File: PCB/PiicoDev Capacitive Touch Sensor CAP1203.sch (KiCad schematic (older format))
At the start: 35 parts, among them J1 , J11 Conn_01x01_Male, J12 Conn_01x01_Male, J13 Conn_01x01_Male, J2 , J3 Conn_PiicoDev_header_01x04_Ma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, J4 Conn_01x01_Male, J5 Conn_01x01_Male, J6 Conn_01x01_Male, J7 Conn_01x01_Male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

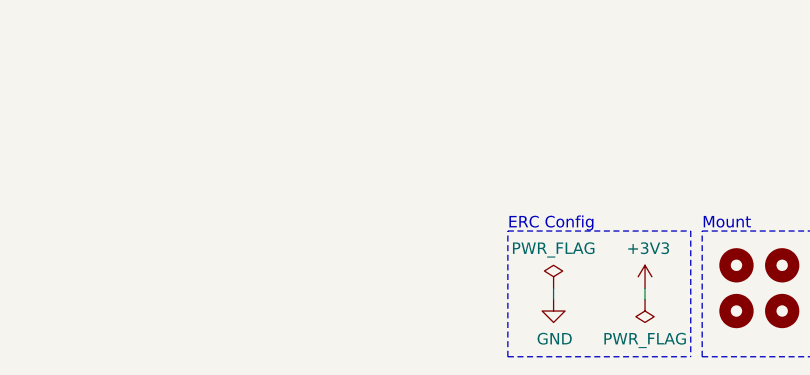
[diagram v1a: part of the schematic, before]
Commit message: Add silk screen labels
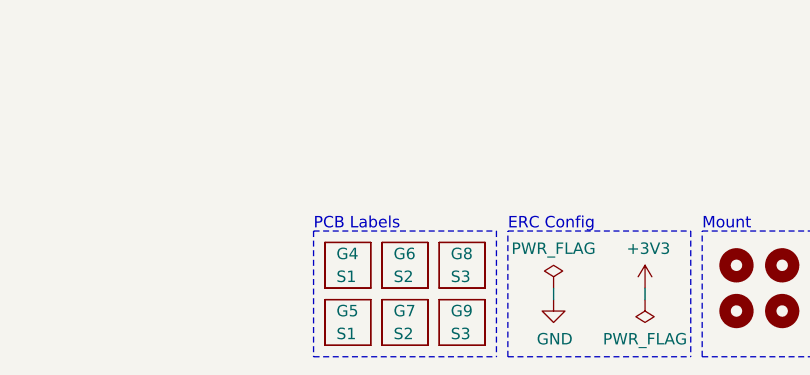
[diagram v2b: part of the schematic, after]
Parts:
- added G4, G5: S1, PiicoDev Capacitive Touch Sensor CAP1203:Label_S1_Reverse, symbol CoreElectronics_Artwork:Label_PCB_Art
- added G6, G7: S2, PiicoDev Capacitive Touch Sensor CAP1203:Label_S2_Reverse, symbol CoreElectronics_Artwork:Label_PCB_Art
- added G8, G9: S3, PiicoDev Capacitive Touch Sensor CAP1203:Label_S3_Reverse, symbol CoreElectronics_Artwork:Label_PCB_Art
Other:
- note added: "PCB Labels"
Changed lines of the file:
@@
 Sheet 1 1
 Title "PiicoDev Capacitive Touch Sensor CAP1203"
-Date "2021-06-09"
-Rev "01"
+Date "2021-06-21"
+Rev "02"
 Comp "Core Electronics"
 Comment1 "Designed at Core Electronics by Peter Johnston"
@@
 	1    0    0    -1
 $EndComp
+$Comp
+L CoreElectronics_Artwork:Label_PCB_Art G5
+U 1 1 60D07939
+P 4450 7600
+F 0 "G5" H 4400 7650 50  0000 L CNN
+F 1 "S1" H 4400 7550 50  0000 L CNN
+F 2 "PiicoDev Capacitive Touch Sensor CAP1203:Label_S1_Reverse" H 4450 7600 50  0001 C CNN
+F 3 "" H 4450 7600 50  0001 C CNN
+	1    4450 7600
+	1    0    0    -1
+$EndComp
+$Comp
+L CoreElectronics_Artwork:Label_PCB_Art G4
+U 1 1 60D089C5
+P 4450 7350
+F 0 "G4" H 4400 7400 50  0000 L CNN
+F 1 "S1" H 4400 7300 50  0000 L CNN
+F 2 "PiicoDev Capacitive Touch Sensor CAP1203:Label_S1_Reverse" H 4450 7350 50  0001 C CNN
+F 3 "" H 4450 7350 50  0001 C CNN
+	1    4450 7350
+	1    0    0    -1
+$EndComp
+$Comp
+L CoreElectronics_Artwork:Label_PCB_Art G6
+U 1 1 60D106CB
+P 4700 7350
+F 0 "G6" H 4650 7400 50  0000 L CNN
+F 1 "S2" H 4650 7300 50  0000 L CNN
+F 2 "PiicoDev Capacitive Touch Sensor CAP1203:Label_S2_Reverse" H 4700 7350 50  0001 C CNN
+F 3 "" H 4700 7350 50  0001 C CNN
+	1    4700 7350
+	1    0    0    -1
+$EndComp
+$Comp
+L CoreElectronics_Artwork:Label_PCB_Art G7
+U 1 1 60D111CB
+P 4700 7600
+F 0 "G7" H 4650 7650 50  0000 L CNN
+F 1 "S2" H 4650 7550 50  0000 L CNN
+F 2 "PiicoDev Capacitive Touch Sensor CAP1203:Label_S2_Reverse" H 4700 7600 50  0001 C CNN
+F 3 "" H 4700 7600 50  0001 C CNN
+	1    4700 7600
+	1    0    0    -1
+$EndComp
+$Comp
+L CoreElectronics_Artwork:Label_PCB_Art G8
+U 1 1 60D11A2F
+P 4950 7350
+F 0 "G8" H 4900 7400 50  0000 L CNN
+F 1 "S3" H 4900 7300 50  0000 L CNN
+F 2 "PiicoDev Capacitive Touch Sensor CAP1203:Label_S3_Reverse" H 4950 7350 50  0001 C CNN
+F 3 "" H 4950 7350 50  0001 C CNN
+	1    4950 7350
+	1    0    0    -1
+$EndComp
+$Comp
+L CoreElectronics_Artwork:Label_PCB_Art G9
+U 1 1 60D121E9
+P 4950 7600
+F 0 "G9" H 4900 7650 50  0000 L CNN
+F 1 "S3" H 4900 7550 50  0000 L CNN
+F 2 "PiicoDev Capacitive Touch Sensor CAP1203:Label_S3_Reverse" H 4950 7600 50  0001 C CNN
+F 3 "" H 4950 7600 50  0001 C CNN
+	1    4950 7600
+	1    0    0    -1
+$EndComp
+Wire Notes Line
+	5100 7200 5100 7750
+Text Notes 4300 7200 0    50   ~ 0
+PCB Labels
+Wire Notes Line
+	4300 7200 4300 7750
+Wire Notes Line
+	4300 7200 5100 7200
+Wire Notes Line
+	4300 7750 5100 7750
 $EndSCHEMATC

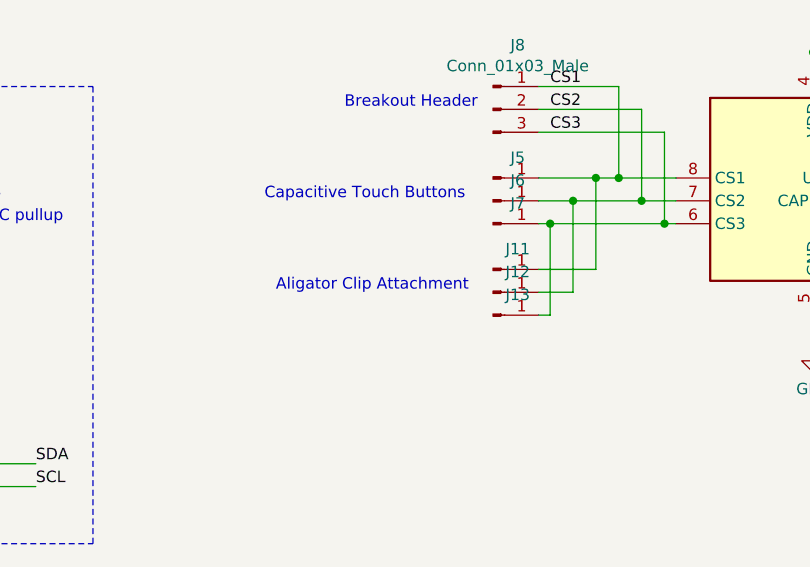
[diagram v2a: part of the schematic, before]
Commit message: Increase Alligator Clip Size
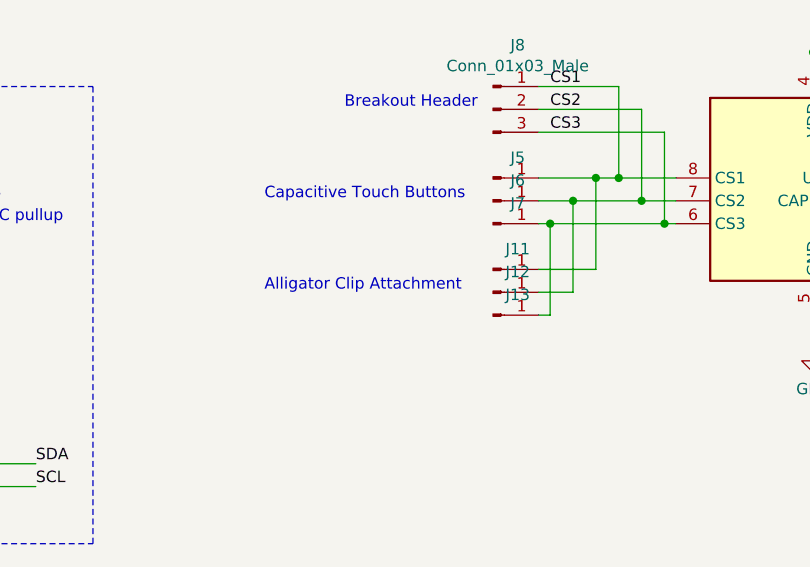
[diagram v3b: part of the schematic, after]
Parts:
- J11, J12, J13: footprint CoreElectronics_Components:Conn_alligator-banana_small -> CoreElectronics_Components:Conn_alligator
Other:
- note added: "Alligator Clip Attachment"
- note removed: "Aligator Clip Attachment"
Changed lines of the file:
@@
 Sheet 1 1
 Title "PiicoDev Capacitive Touch Sensor CAP1203"
-Date "2021-06-21"
+Date "2021-06-24"
 Rev "02"
 Comp "Core Electronics"
@@
 F 0 "J11" H 5808 3889 50  0000 C CNN
 F 1 "Conn_01x01_Male" H 5808 3890 50  0001 C CNN
-F 2 "CoreElectronics_Components:Conn_alligator-banana_small" H 5700 3800 50  0001 C CNN
+F 2 "CoreElectronics_Components:Conn_alligator" H 5700 3800 50  0001 C CNN
 F 3 "~" H 5700 3800 50  0001 C CNN
 	1    5700 3800
@@
 F 0 "J12" H 5808 3989 50  0000 C CNN
 F 1 "Conn_01x01_Male" H 5808 3990 50  0001 C CNN
-F 2 "CoreElectronics_Components:Conn_alligator-banana_small" H 5700 3900 50  0001 C CNN
+F 2 "CoreElectronics_Components:Conn_alligator" H 5700 3900 50  0001 C CNN
 F 3 "~" H 5700 3900 50  0001 C CNN
 	1    5700 3900
@@
 F 0 "J13" H 5808 4089 50  0000 C CNN
 F 1 "Conn_01x01_Male" H 5808 4090 50  0001 C CNN
-F 2 "CoreElectronics_Components:Conn_alligator-banana_small" H 5700 4000 50  0001 C CNN
+F 2 "CoreElectronics_Components:Conn_alligator" H 5700 4000 50  0001 C CNN
 F 3 "~" H 5700 4000 50  0001 C CNN
 	1    5700 4000
@@
 Text Notes 5050 3100 0    50   ~ 0
 Breakout Header
-Text Notes 4750 3900 0    50   ~ 0
-Aligator Clip Attachment
+Text Notes 4700 3900 0    50   ~ 0
+Alligator Clip Attachment
 $Comp
 L Jumper:SolderJumper_2_Bridged JP4

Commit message: Change R1 resistor value
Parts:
- R1: value 1k -> 4k7
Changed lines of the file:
@@
 AR Path="/60B035C6" Ref="R1"  Part="1"
 F 0 "R1" H 1520 3996 50  0000 L CNN
-F 1 "1k" H 1520 3905 50  0000 L CNN
+F 1 "4k7" H 1520 3905 50  0000 L CNN
 F 2 "Resistor_SMD:R_0402_1005Metric" V 1380 3950 50  0001 C CNN
 F 3 "~" H 1450 3950 50  0001 C CNN

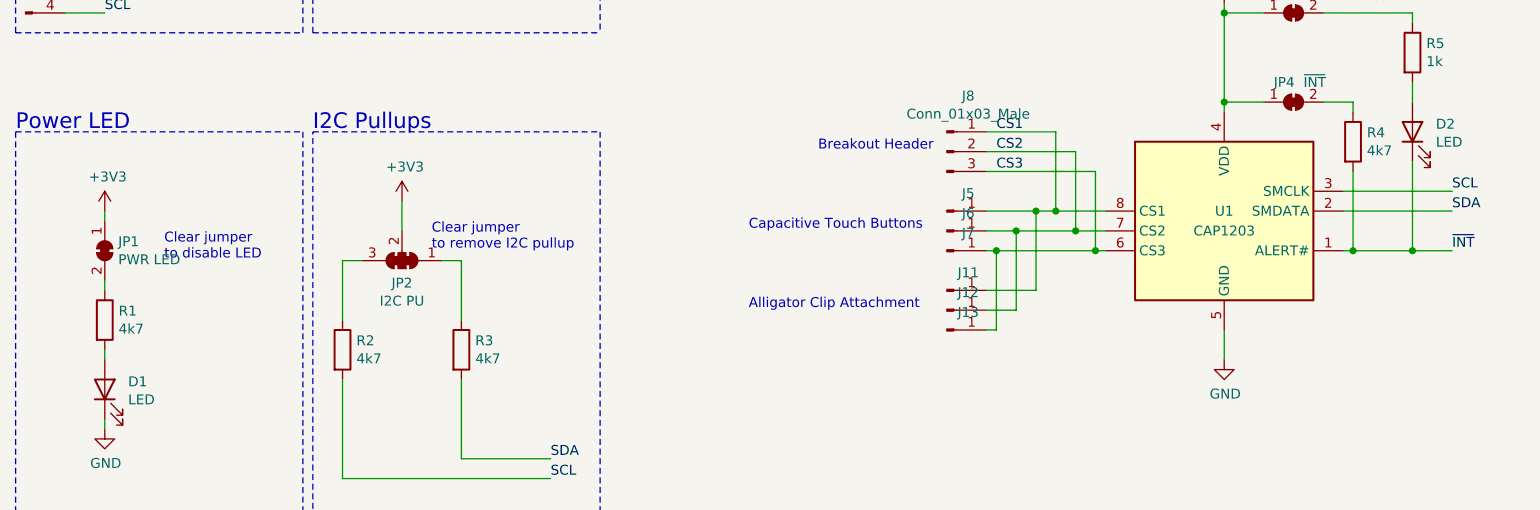
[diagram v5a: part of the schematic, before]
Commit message: Update R1,2,3,4 to 10k
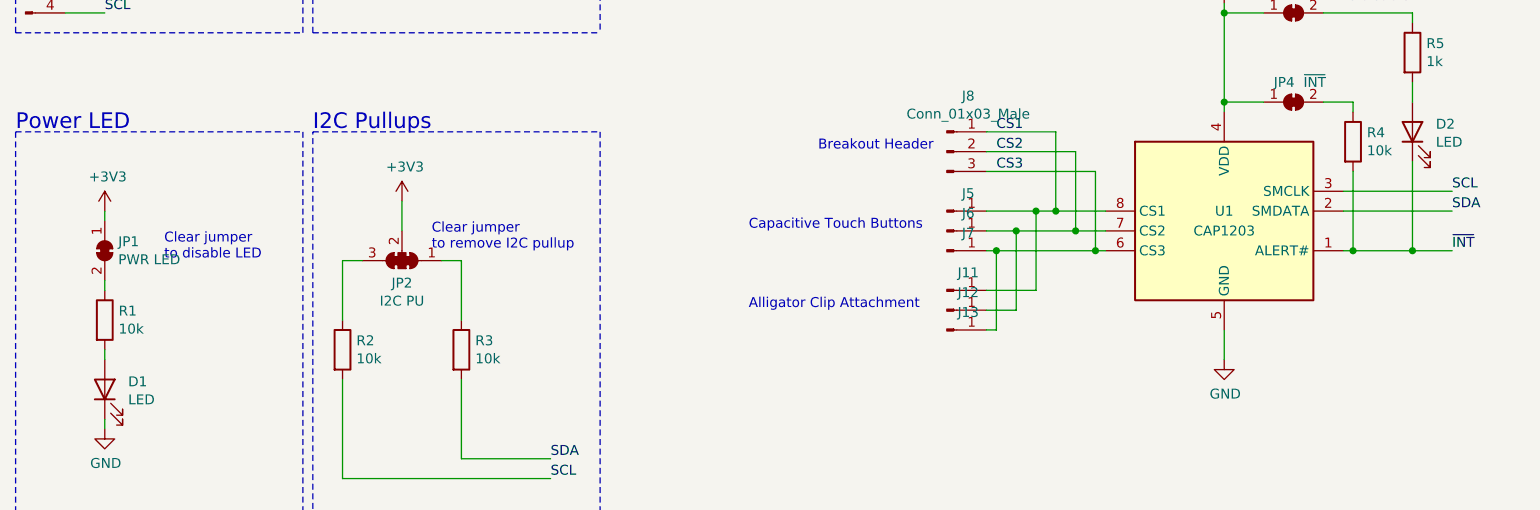
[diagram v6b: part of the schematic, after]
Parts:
- R1, R2, R3, R4: value 4k7 -> 10k
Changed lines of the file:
@@
 P 5350 7450
 AR Path="/609C5735/609C9ECA" Ref="#FLG?"  Part="1"
-AR Path="/609C9ECA" Ref="#FLG0101"  Part="1"
-F 0 "#FLG0101" H 5350 7525 50  0001 C CNN
+AR Path="/609C9ECA" Ref="#FLG?"  Part="1"
+F 0 "#FLG?" H 5350 7525 50  0001 C CNN
 F 1 "PWR_FLAG" H 5350 7623 50  0000 C CNN
 F 2 "" H 5350 7450 50  0001 C CNN
@@
 P 5750 7500
 AR Path="/609C5735/609C9ED0" Ref="#FLG?"  Part="1"
-AR Path="/609C9ED0" Ref="#FLG0102"  Part="1"
-F 0 "#FLG0102" H 5750 7575 50  0001 C CNN
+AR Path="/609C9ED0" Ref="#FLG?"  Part="1"
+F 0 "#FLG?" H 5750 7575 50  0001 C CNN
 F 1 "PWR_FLAG" H 5750 7673 50  0000 C CNN
 F 2 "" H 5750 7500 50  0001 C CNN
@@
 P 5350 7500
 AR Path="/609C5735/609C9ED6" Ref="#PWR?"  Part="1"
-AR Path="/609C9ED6" Ref="#PWR0101"  Part="1"
-F 0 "#PWR0101" H 5350 7250 50  0001 C CNN
+AR Path="/609C9ED6" Ref="#PWR?"  Part="1"
+F 0 "#PWR?" H 5350 7250 50  0001 C CNN
 F 1 "GND" H 5355 7327 50  0000 C CNN
 F 2 "" H 5350 7500 50  0001 C CNN
@@
 P 5750 7450
 AR Path="/609C5735/609C9EDC" Ref="#PWR?"  Part="1"
-AR Path="/609C9EDC" Ref="#PWR0102"  Part="1"
-F 0 "#PWR0102" H 5750 7300 50  0001 C CNN
+AR Path="/609C9EDC" Ref="#PWR?"  Part="1"
+F 0 "#PWR?" H 5750 7300 50  0001 C CNN
 F 1 "+3V3" H 5765 7623 50  0000 C CNN
 F 2 "" H 5750 7450 50  0001 C CNN
@@
 P 1600 1400
 AR Path="/609C5735/609F9AF4" Ref="#PWR?"  Part="1"
-AR Path="/609F9AF4" Ref="#PWR0103"  Part="1"
-F 0 "#PWR0103" H 1600 1250 50  0001 C CNN
+AR Path="/609F9AF4" Ref="#PWR?"  Part="1"
+F 0 "#PWR?" H 1600 1250 50  0001 C CNN
 F 1 "+3V3" V 1615 1528 50  0000 L CNN
 F 2 "" H 1600 1400 50  0001 C CNN
@@
 P 1600 1300
 AR Path="/609C5735/609F9AFA" Ref="#PWR?"  Part="1"
-AR Path="/609F9AFA" Ref="#PWR0104"  Part="1"
-F 0 "#PWR0104" H 1600 1050 50  0001 C CNN
+AR Path="/609F9AFA" Ref="#PWR?"  Part="1"
+F 0 "#PWR?" H 1600 1050 50  0001 C CNN
 F 1 "GND" V 1605 1172 50  0000 R CNN
 F 2 "" H 1600 1300 50  0001 C CNN
@@
 P 1600 2200
 AR Path="/609C5735/609F9B0C" Ref="#PWR?"  Part="1"
-AR Path="/609F9B0C" Ref="#PWR0105"  Part="1"
-F 0 "#PWR0105" H 1600 2050 50  0001 C CNN
+AR Path="/609F9B0C" Ref="#PWR?"  Part="1"
+F 0 "#PWR?" H 1600 2050 50  0001 C CNN
 F 1 "+3V3" V 1615 2328 50  0000 L CNN
 F 2 "" H 1600 2200 50  0001 C CNN
@@
 P 1600 2100
 AR Path="/609C5735/609F9B12" Ref="#PWR?"  Part="1"
-AR Path="/609F9B12" Ref="#PWR0106"  Part="1"
-F 0 "#PWR0106" H 1600 1850 50  0001 C CNN
+AR Path="/609F9B12" Ref="#PWR?"  Part="1"
+F 0 "#PWR?" H 1600 1850 50  0001 C CNN
 F 1 "GND" V 1605 1972 50  0000 R CNN
 F 2 "" H 1600 2100 50  0001 C CNN
@@
 P 3300 1400
 AR Path="/609C5735/609F9B1E" Ref="#PWR?"  Part="1"
-AR Path="/609F9B1E" Ref="#PWR0107"  Part="1"
-F 0 "#PWR0107" H 3300 1250 50  0001 C CNN
+AR Path="/609F9B1E" Ref="#PWR?"  Part="1"
+F 0 "#PWR?" H 3300 1250 50  0001 C CNN
 F 1 "+3V3" V 3315 1528 50  0000 L CNN
 F 2 "" H 3300 1400 50  0001 C CNN
@@
 P 3300 1300
 AR Path="/609C5735/609F9B24" Ref="#PWR?"  Part="1"
-AR Path="/609F9B24" Ref="#PWR0108"  Part="1"
-F 0 "#PWR0108" H 3300 1050 50  0001 C CNN
+AR Path="/609F9B24" Ref="#PWR?"  Part="1"
+F 0 "#PWR?" H 3300 1050 50  0001 C CNN
 F 1 "GND" V 3305 1172 50  0000 R CNN
 F 2 "" H 3300 1300 50  0001 C CNN
@@
 AR Path="/60A08162" Ref="R3"  Part="1"
 F 0 "R3" H 3320 4146 50  0000 L CNN
-F 1 "4k7" H 3320 4055 50  0000 L CNN
+F 1 "10k" H 3320 4055 50  0000 L CNN
 F 2 "Resistor_SMD:R_0402_1005Metric" V 3180 4100 50  0001 C CNN
 F 3 "~" H 3250 4100 50  0001 C CNN
@@
 AR Path="/60A08170" Ref="R2"  Part="1"
 F 0 "R2" H 2720 4146 50  0000 L CNN
-F 1 "4k7" H 2720 4055 50  0000 L CNN
+F 1 "10k" H 2720 4055 50  0000 L CNN
 F 2 "Resistor_SMD:R_0402_1005Metric" V 2580 4100 50  0001 C CNN
 F 3 "~" H 2650 4100 50  0001 C CNN
@@
 P 2950 3350
 AR Path="/609C5735/60A0817C" Ref="#PWR?"  Part="1"
-AR Path="/60A0817C" Ref="#PWR0109"  Part="1"
-F 0 "#PWR0109" H 2950 3200 50  0001 C CNN
+AR Path="/60A0817C" Ref="#PWR?"  Part="1"
+F 0 "#PWR?" H 2950 3200 50  0001 C CNN
 F 1 "+3V3" H 2965 3523 50  0000 C CNN
 F 2 "" H 2950 3350 50  0001 C CNN
@@
 	1000 5000 2450 5000
 $Comp
-L power:+3V3 #PWR0112
+L power:+3V3 #PWR?
 U 1 1 60A58B8E
 P 7100 2350
-F 0 "#PWR0112" H 7100 2200 50  0001 C CNN
+F 0 "#PWR?" H 7100 2200 50  0001 C CNN
 F 1 "+3V3" H 7115 2523 50  0000 C CNN
 F 2 "" H 7100 2350 50  0001 C CNN
@@
 ~INT
 $Comp
-L power:GND #PWR0113
+L power:GND #PWR?
 U 1 1 60A63B22
 P 7100 4150
-F 0 "#PWR0113" H 7100 3900 50  0001 C CNN
+F 0 "#PWR?" H 7100 3900 50  0001 C CNN
 F 1 "GND" H 7105 3977 50  0000 C CNN
 F 2 "" H 7100 4150 50  0001 C CNN
@@
 Connection ~ 9000 3700
 $Comp
-L power:GND #PWR0114
+L power:GND #PWR?
 U 1 1 60A78BAC
 P 9000 4150
-F 0 "#PWR0114" H 9000 3900 50  0001 C CNN
+F 0 "#PWR?" H 9000 3900 50  0001 C CNN
 F 1 "GND" H 9005 3977 50  0000 C CNN
 F 2 "" H 9000 4150 50  0001 C CNN
@@
 $EndComp
 $Comp
-L power:+3V3 #PWR0115
+L power:+3V3 #PWR?
 U 1 1 60A790DA
 P 9000 3650
-F 0 "#PWR0115" H 9000 3500 50  0001 C CNN
+F 0 "#PWR?" H 9000 3500 50  0001 C CNN
 F 1 "+3V3" H 9015 3823 50  0000 C CNN
 F 2 "" H 9000 3650 50  0001 C CNN
@@
 AR Path="/60A7A47E" Ref="R4"  Part="1"
 F 0 "R4" H 7820 3096 50  0000 L CNN
-F 1 "4k7" H 7820 3005 50  0000 L CNN
+F 1 "10k" H 7820 3005 50  0000 L CNN
 F 2 "Resistor_SMD:R_0402_1005Metric" V 7680 3050 50  0001 C CNN
 F 3 "~" H 7750 3050 50  0001 C CNN
@@
 P 1450 4500
 AR Path="/60AFFD09/60B035B2" Ref="#PWR?"  Part="1"
-AR Path="/60B035B2" Ref="#PWR0110"  Part="1"
-F 0 "#PWR0110" H 1450 4250 50  0001 C CNN
+AR Path="/60B035B2" Ref="#PWR?"  Part="1"
+F 0 "#PWR?" H 1450 4250 50  0001 C CNN
 F 1 "GND" H 1455 4327 50  0000 C CNN
 F 2 "" H 1450 4500 50  0001 C CNN
@@
 P 1450 3400
 AR Path="/60AFFD09/60B035B9" Ref="#PWR?"  Part="1"
-AR Path="/60B035B9" Ref="#PWR0111"  Part="1"
-F 0 "#PWR0111" H 1450 3250 50  0001 C CNN
+AR Path="/60B035B9" Ref="#PWR?"  Part="1"
+F 0 "#PWR?" H 1450 3250 50  0001 C CNN
 F 1 "+3V3" H 1465 3573 50  0000 C CNN
 F 2 "" H 1450 3400 50  0001 C CNN
@@
 AR Path="/60B035C6" Ref="R1"  Part="1"
 F 0 "R1" H 1520 3996 50  0000 L CNN
-F 1 "4k7" H 1520 3905 50  0000 L CNN
+F 1 "10k" H 1520 3905 50  0000 L CNN
 F 2 "Resistor_SMD:R_0402_1005Metric" V 1380 3950 50  0001 C CNN
 F 3 "~" H 1450 3950 50  0001 C CNN
